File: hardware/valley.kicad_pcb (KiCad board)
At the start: 2 copper layers, 71 x 42.8 mm, 29 parts, among them IC1 TLC5971_SOP, P2 USB_OTG, P4 CONN_01X16, Q1 PDTD113ZT,215, Q2 BSS138, Q3 PDTD113ZT,215, U1 CH341A, U2 AP111733, U3 ESP-12E, Y1 12M

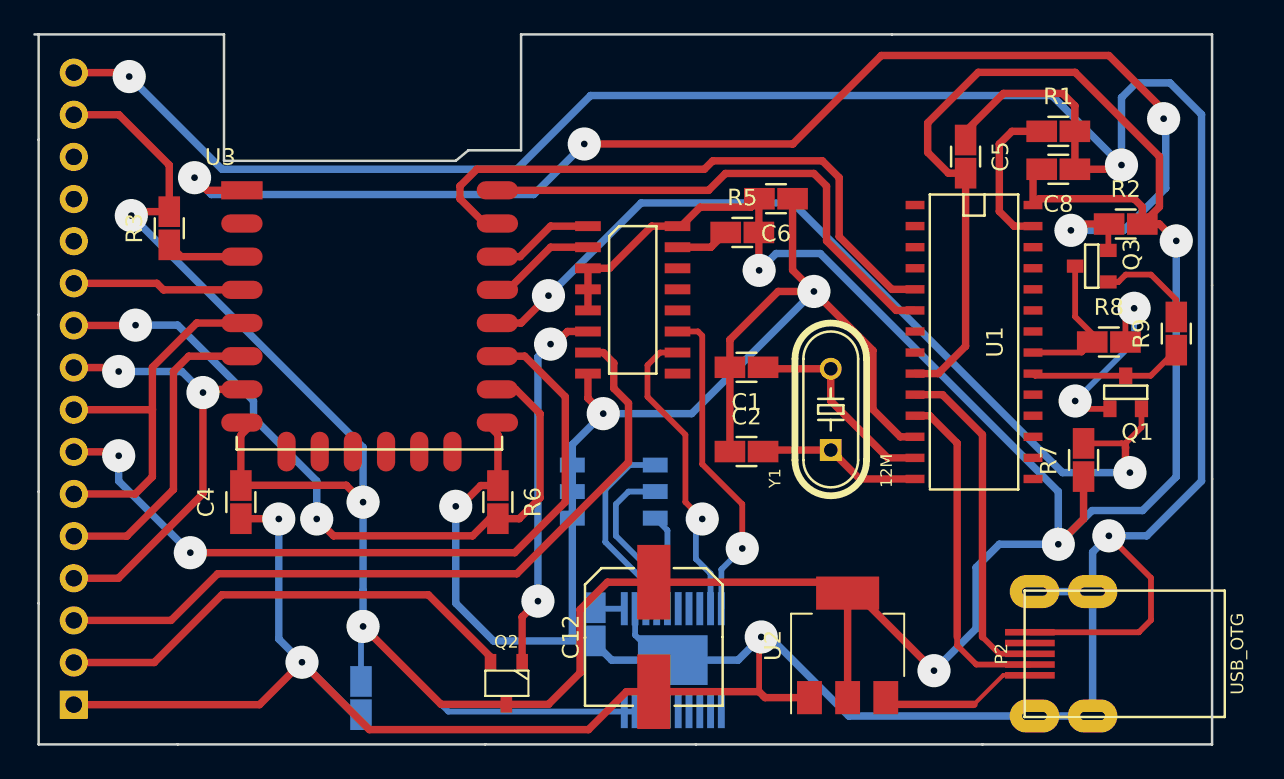
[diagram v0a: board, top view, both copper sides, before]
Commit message: Updating to use ESP32 as main processor -- no need of the separate LED driver or I2C IO expander.
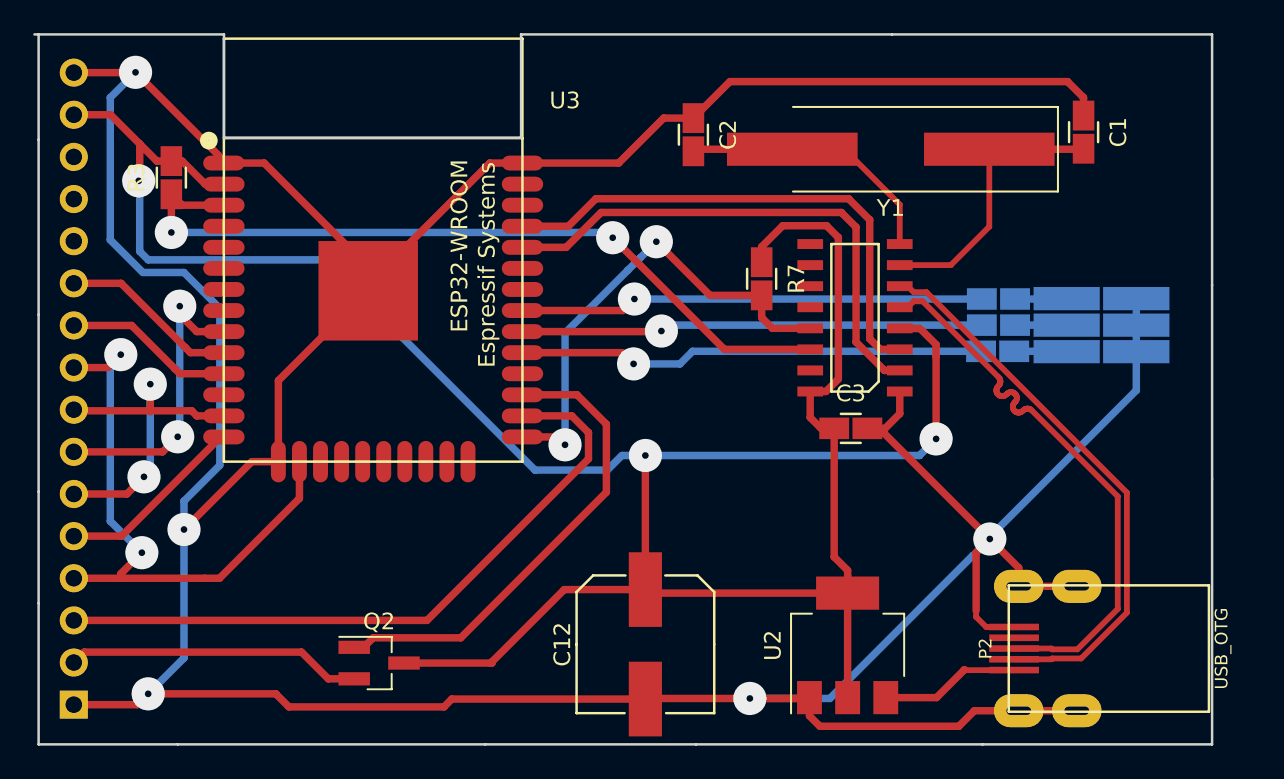
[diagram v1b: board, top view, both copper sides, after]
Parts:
- removed ??1: PCA9557, adamgreig/agg-kicad/agg.pretty:SOIC-16
- removed C4, C5, C6, C8: 0.1u, coddingtonbear/coddingtonbear.pretty:0805_Milling
- removed IC1: TLC5971_SOP, brunoeagle/kicad-open-modules:TSSOP-20
- removed Q1, Q3: PDTD113ZT,215, celeritous/KiCad.pretty:SOT23-3
- removed R2, R8, R9: 10k, coddingtonbear/coddingtonbear.pretty:0805_Milling
- removed R6: 100k, coddingtonbear/coddingtonbear.pretty:0805_Milling
- C3: moved to F.Cu
- D1: footprint valley:SLV6A-FKB -> coddingtonbear/coddingtonbear.pretty:SLV6A-FKB-MILLING
- Q2: footprint cbrues/kicad-lib2/footprints/sm-ics.pretty:SM-SOT23 -> KiCad/TO_SOT_Packages_SMD.pretty:SOT-23_Handsoldering
- R1: value R -> 10k; moved to B.Cu
- R4: value 5k -> 10k
- R5: value 2k -> 10k; moved to B.Cu
- R7: value 4.7k -> 10k
- U1: value CH341A -> CH340G; footprint KiCad/SMD_Packages.pretty:SOIC-28 -> adamgreig/agg-kicad/agg.pretty:SOIC-16
- U3: value ESP-12E -> ESP32-WROOM; footprint coddingtonbear/coddingtonbear.pretty:ESP-12E -> adamjvr/ESP32-kiCAD-Footprints/ESP32-Footprints/ESP32-footprints-Lib.pretty:ESP32-WROOM
- Y1: footprint monostable/CommonPartsLibrary.pretty:XTAL_HC-49US-16.000MHZ -> KiCad/Crystals.pretty:Crystal_SMD_HC49-SD_HandSoldering
- moved C3 33.7 mm to (168.3, 61.6), turned to 0 degrees
- moved D1 31.1 mm to (183.5, 55.4), turned to 180 degrees
- moved R4 30.3 mm to (177.2, 55.4), turned to 180 degrees
- moved C1 24.8 mm to (182.4, 43.7), turned to 270 degrees
- moved R7 22.3 mm to (163.0, 52.6), turned to 270 degrees
- moved C2 19.4 mm to (158.9, 43.9), turned to 270 degrees
- moved R5 17.0 mm to (177.2, 56.9), turned to 180 degrees
- moved Y1 16.1 mm to (170.8, 44.8), turned to 180 degrees
- moved R1 10.7 mm to (177.2, 53.8), turned to 180 degrees
- moved U3 8.07 mm to (139.5, 50.9), turned to 180 degrees
- moved Q2 7.77 mm to (139.9, 75.7), turned to 0 degrees
- moved U1 7.32 mm to (168.6, 54.9), turned to 180 degrees
- moved R3 3.05 mm to (127.4, 46.5)
- moved P2 1.00 mm to (177.9, 74.9)
- moved C12 0.68 mm to (156.0, 74.6)
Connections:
- C1 pad 1: Net-(C1-Pad1) -> GND
- C1 pad 2: GND -> Net-(C1-Pad2)
- C3 pad 1: GND -> +3V3
- C3 pad 2: +3V3 -> GND
- D1 pad 4: LED_BLUE -> Net-(D1-Pad4)
- D1 pad 5: LED_GREEN -> Net-(D1-Pad5)
- D1 pad 6: LED_RED -> Net-(D1-Pad6)
- R1 pad 1: Net-(R1-Pad1) -> Net-(D1-Pad4)
- R1 pad 2: GND -> LED_BLUE
- R3 pad 1: Net-(R3-Pad1) -> RTS
- R4 pad 1: Net-(IC1-Pad1) -> Net-(D1-Pad5)
- R4 pad 2: GND -> LED_GREEN
- R5 pad 1: Net-(??1-Pad15) -> Net-(D1-Pad6)
- R5 pad 2: +3V3 -> LED_RED
- R7 pad 2: GPIO0 -> DTR
- U1 pad 1: Net-(U1-Pad1) -> GND
- U1 pad 10: UD+ -> Net-(U1-Pad10)
- U1 pad 11: UD- -> Net-(U1-Pad11)
- U1 pad 12: GND -> Net-(U1-Pad12)
- U1 pad 13: Net-(C1-Pad1) -> DTR
- U1 pad 14: Net-(C2-Pad2) -> RTS
- U1 pad 16: Net-(U1-Pad16) -> +3V3
- U1 pad 2: Net-(U1-Pad2) -> RXD
- U1 pad 3: Net-(U1-Pad3) -> TXD
- U1 pad 4: Net-(U1-Pad4) -> +3V3
- U1 pad 5: RXD -> UD+
- U1 pad 6: TXD -> UD-
- U1 pad 7: Net-(U1-Pad7) -> Net-(C1-Pad2)
- U1 pad 8: Net-(U1-Pad8) -> Net-(C2-Pad2)
- U1 pad 9: +3V3 -> Net-(U1-Pad9)
- U3 pad 1: REST -> GND
- U3 pad 10: A0 -> RESET_TFT
- U3 pad 11: CS_TFT -> A0
- U3 pad 12: GPIO0 -> Net-(U3-Pad12)
- U3 pad 13: SDA -> SCK
- U3 pad 14: SCL -> MISO
- U3 pad 15: RXD -> GND
- U3 pad 16: TXD -> MOSI
- U3 pad 2: Net-(U3-Pad2) -> +3V3
- U3 pad 3: Net-(R3-Pad1) -> RTS
- U3 pad 4: RESET_TFT -> Net-(U3-Pad4)
- U3 pad 5: SCK -> Net-(U3-Pad5)
- U3 pad 6: MISO -> Net-(U3-Pad6)
- U3 pad 7: MOSI -> Net-(U3-Pad7)
- U3 pad 8: +3V3 -> Net-(U3-Pad8)
- U3 pad 9: GND -> CS_TFT
- Y1 pad 1: Net-(C2-Pad2) -> Net-(C1-Pad2)
- Y1 pad 2: Net-(C1-Pad1) -> Net-(C2-Pad2)
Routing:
- net +3V3: track 267.9 -> 153.4 mm, vias 7 -> 3
- net REST: track 83.1 -> 0.00 mm, vias 4 -> 0
- net GND: track 345.9 -> 268.1 mm, vias 9 -> 5
- net GPIO0: track 55.5 -> 0.00 mm, vias 2 -> 0
- net RTS: track 8.12 -> 47.7 mm, vias 0 -> 2
- net A0: track 45.2 -> 10.3 mm, vias 2 -> 0
- net CS_TFT: track 46.5 -> 18.2 mm
- net LED_BLUE: track 5.77 -> 28.0 mm, vias 0 -> 1
- net DTR: track 9.33 -> 29.5 mm, vias 0 -> 2
- net Net-(??1-Pad11): track 19.6 -> 0.00 mm, vias 1 -> 0
- net Net-(??1-Pad10): track 18.7 -> 0.00 mm, vias 1 -> 0
- net LED_GREEN: track 10.0 -> 27.9 mm, vias 0 -> 1
- net Net-(C1-Pad2): track 0.00 -> 16.7 mm
- net LED_RED: track 11.8 -> 28.2 mm, vias 0 -> 1
- net UD-: track 20.3 -> 34.0 mm
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- removed copper zone on F.Cu, net (none)
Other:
- outline, holes or cut-outs redrawn
- net class Default: clearance 0.2 -> 0.19
- net class Power: clearance 0.2 -> 0.19
- rule trace_clearance: 0.2 -> 0.19

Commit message: Swapping CH340G to CH341A
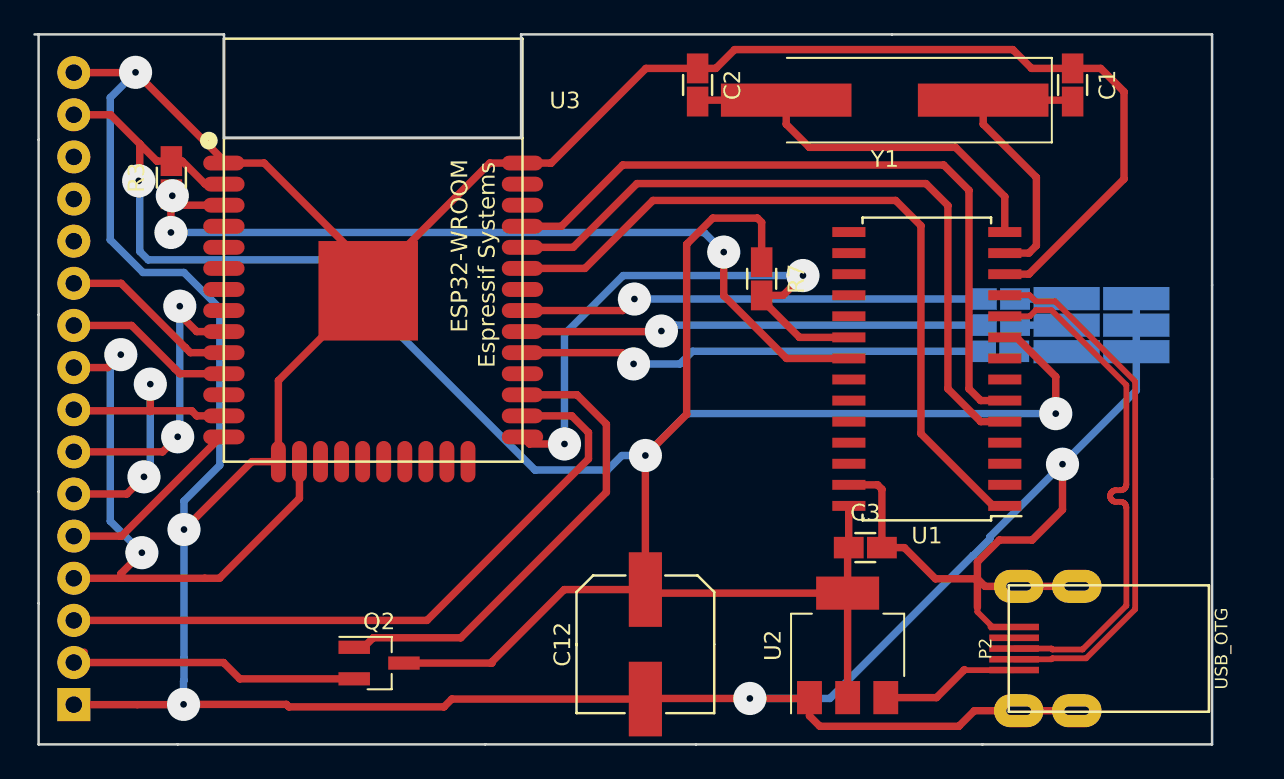
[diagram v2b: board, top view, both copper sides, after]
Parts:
- U1: value CH340G -> CH341A; footprint adamgreig/agg-kicad/agg.pretty:SOIC-16 -> KiCad/Housings_SOIC.pretty:SOIC-28W_7.5x17.9mm_Pitch1.27mm
- moved C3 7.24 mm to (169.2, 68.8)
- moved U1 5.32 mm to (172.9, 58.0)
- moved C2 3.01 mm to (159.1, 40.9)
- moved Y1 2.98 mm to (170.4, 41.8)
- moved C1 2.92 mm to (181.7, 40.9)
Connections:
- net Net-(P4-Pad2) renamed /BACKLIGHT_3V3
- U1 pad 1: GND -> USB_CONNECTED
- U1 pad 10: Net-(U1-Pad10) -> UD+
- U1 pad 11: Net-(U1-Pad11) -> UD-
- U1 pad 12: Net-(U1-Pad12) -> GND
- U1 pad 13: DTR -> Net-(C1-Pad2)
- U1 pad 14: RTS -> Net-(C2-Pad2)
- U1 pad 16: +3V3 -> Net-(U1-Pad16)
- U1 pad 2: RXD -> Net-(U1-Pad2)
- U1 pad 3: TXD -> Net-(U1-Pad3)
- U1 pad 4: +3V3 -> Net-(U1-Pad4)
- U1 pad 5: UD+ -> RXD
- U1 pad 6: UD- -> TXD
- U1 pad 7: Net-(C1-Pad2) -> Net-(U1-Pad7)
- U1 pad 8: Net-(C2-Pad2) -> Net-(U1-Pad8)
- U1 pad 9: Net-(U1-Pad9) -> +3V3
- U3 pad 33: Net-(U3-Pad33) -> USB_CONNECTED
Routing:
- net USB_CONNECTED: track 0.00 -> 45.7 mm
- net GND: track 268.1 -> 289.7 mm
- net TXD: track 31.4 -> 43.5 mm
- net RXD: track 31.6 -> 43.1 mm
- net Net-(C2-Pad2): track 16.3 -> 23.9 mm
- net DTR: track 29.5 -> 34.6 mm
- net RTS: track 47.7 -> 51.7 mm, vias 2 -> 3
- net UD+: track 34.0 -> 31.9 mm
- net +3V3: track 153.4 -> 155.5 mm
- net UD-: track 34.0 -> 32.3 mm
- net Net-(C1-Pad2): track 16.7 -> 17.6 mm

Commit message: Setting reference point.
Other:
- net class Default: trace_width 0.45 -> 0.25
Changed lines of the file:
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@@
-(kicad_pcb (version 20170920) (host pcbnew "(2017-09-25 revision 6e440ff)-master")
+(kicad_pcb (version 20170123) (host pcbnew no-vcs-found-e2505cb~60~ubuntu16.04.1)
   (general
     (thickness 1.6)
@@
   )
   (setup
-    (last_trace_width 0.45)
+    (last_trace_width 0.25)
     (user_trace_width 0.35)
     (trace_clearance 0.19)
@@
     (pad_drill 0.762)
     (pad_to_mask_clearance 0.2)
-    (aux_axis_origin 0 0)
+    (aux_axis_origin 119.38 80.645)
     (visible_elements FFFFFF7F)
     (pcbplotparams
@@
       (outputformat 1)
       (mirror false)
-      (drillshape 1)
+      (drillshape 0)
       (scaleselection 1)
       (outputdirectory ""))
@@
   (net_class Default "This is the default net class."
     (clearance 0.19)
-    (trace_width 0.45)
+    (trace_width 0.25)
     (via_dia 2)
     (via_drill 0.4)

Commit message: Minor schematic updates.
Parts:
- removed Q2: BSS138, KiCad/TO_SOT_Packages_SMD.pretty:SOT-23_Handsoldering
- R1, R4: value 10k -> 10
- R5: value 10k -> 150
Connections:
- P4 pad 2: /BACKLIGHT_3V3 -> +3V3
- U3 pad 27: BACKLIGHT -> Net-(U3-Pad27)
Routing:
- net BACKLIGHT: track 29.0 -> 0.00 mm
- net +3V3: track 155.5 -> 176.4 mm
- net /BACKLIGHT_3V3: track 18.4 -> 0.00 mm
- net RTS: vias 3 -> 2
